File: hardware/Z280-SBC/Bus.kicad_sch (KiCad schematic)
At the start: 5 parts, among them J4 ATF-JTAG-10, J5 Conn_02x10_Odd_Even, J6 ADBUS, J7 SIGBUS, U10 ATF1504AS-10JU84

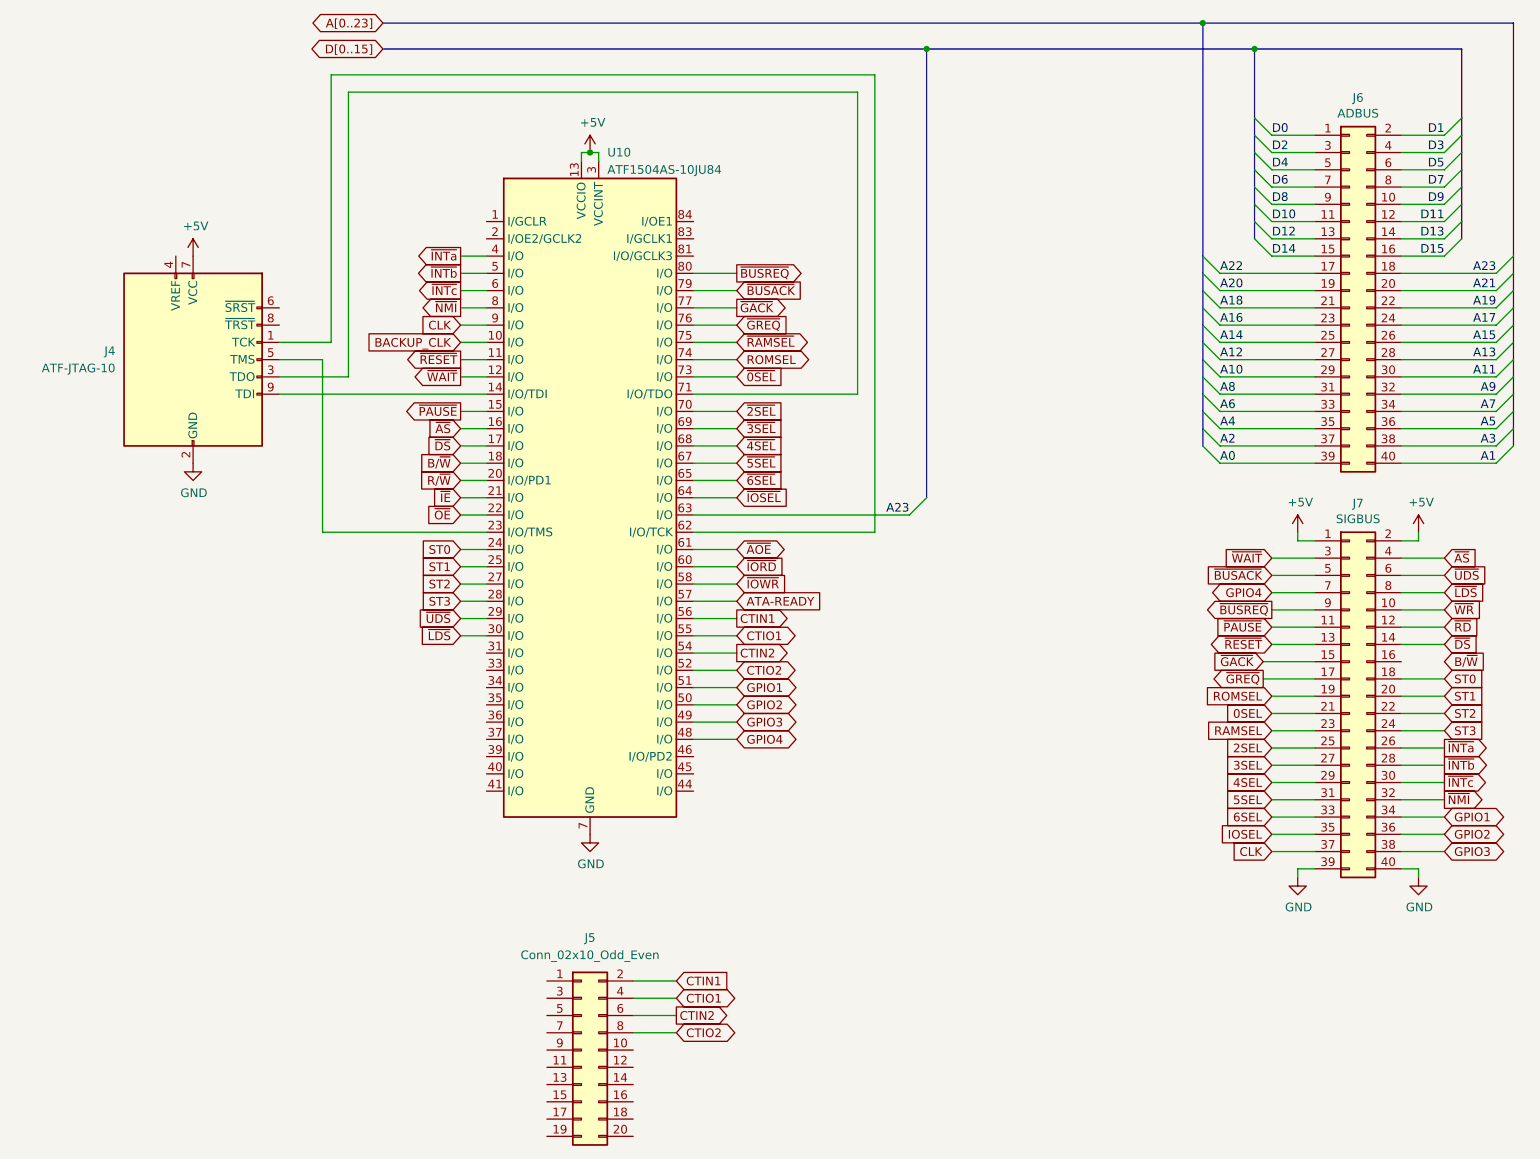
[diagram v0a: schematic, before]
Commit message: Work in progress on PCB design, address and data buses mostly connected
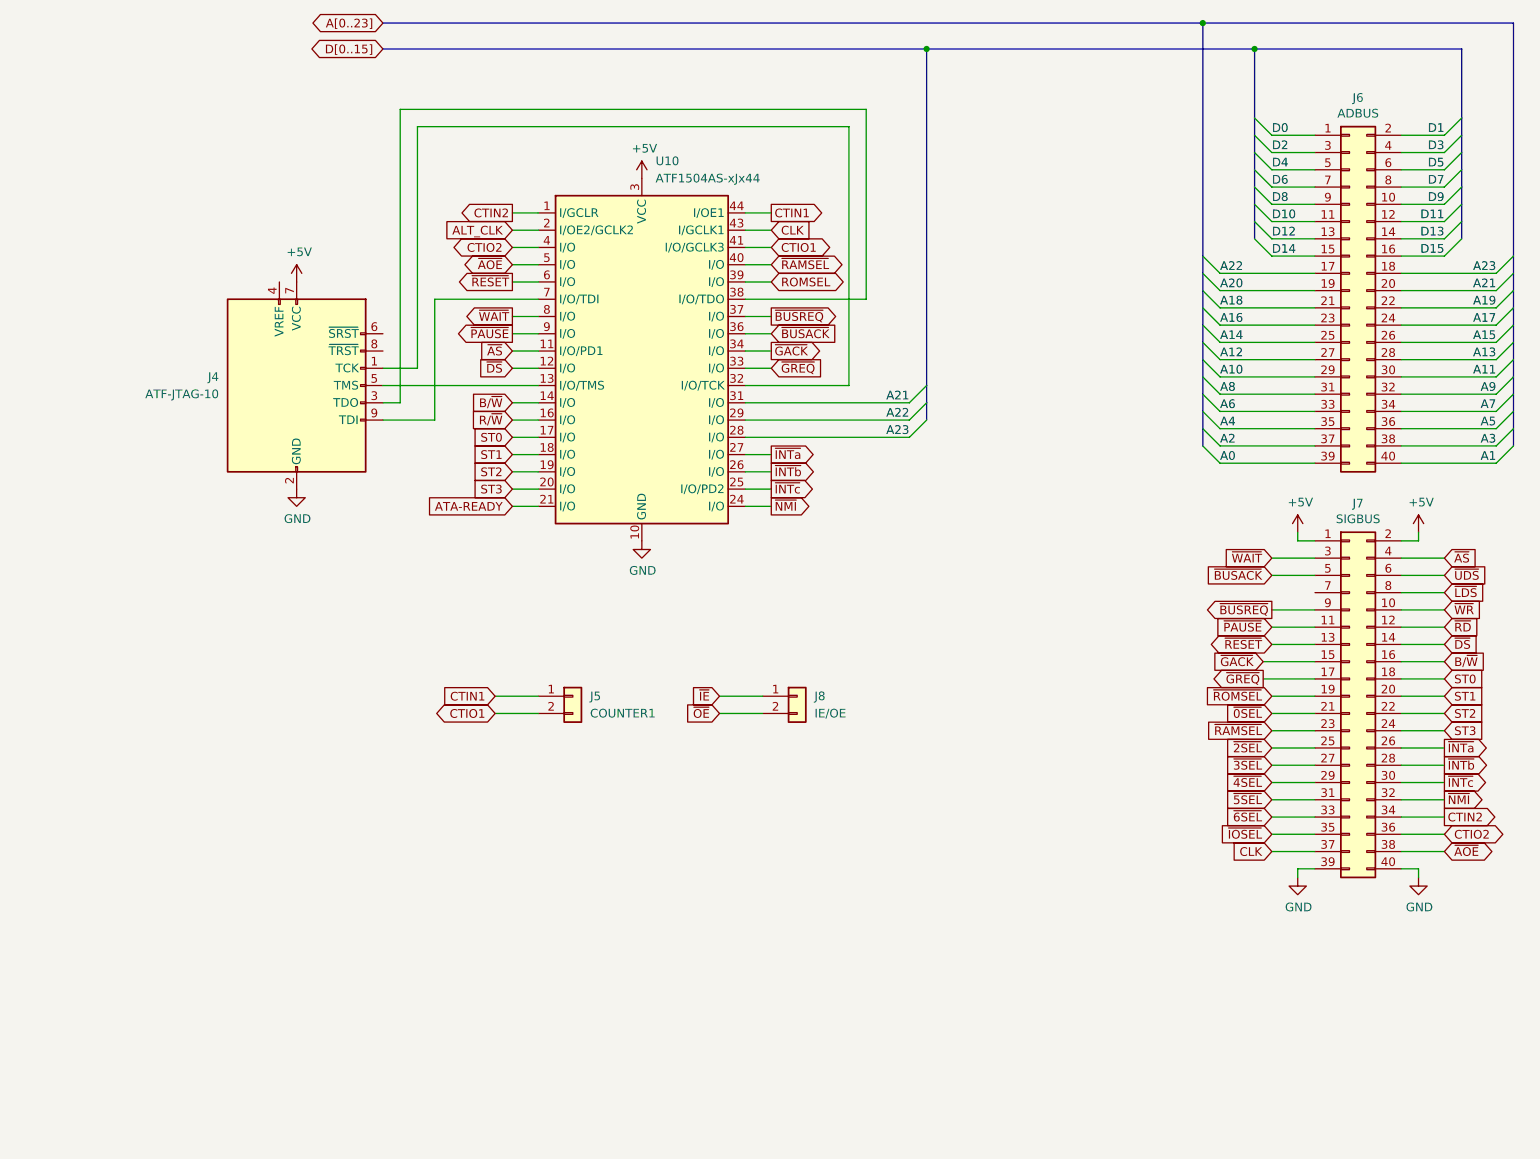
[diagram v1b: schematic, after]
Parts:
- removed J5: Conn_02x10_Odd_Even, Connector_PinHeader_2.54mm:PinHeader_2x10_P2.54mm_Vertical, symbol Connector_Generic:Conn_02x10_Odd_Even
- removed U10: ATF1504AS-10JU84, Package_LCC:PLCC-84_THT-Socket, symbol Z280:ATF1504AS-10JU84
- added J5: COUNTER1, Connector_PinHeader_2.54mm:PinHeader_1x02_P2.54mm_Vertical, symbol Connector_Generic:Conn_01x02
- added J8: IE/OE, Connector_PinHeader_2.54mm:PinHeader_1x02_P2.54mm_Vertical, symbol Connector_Generic:Conn_01x02
- added U10: ATF1504AS-xJx44, Package_LCC:PLCC-44_THT-Socket, symbol Z280:ATF1504AS-xJx44
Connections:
- net 0SEL is gone; now on net ~{0SEL}: J7.21 (Pin_21)
- net 2SEL is gone; now on net ~{2SEL}: J7.25 (Pin_25)
- net 3SEL is gone; now on net ~{3SEL}: J7.27 (Pin_27)
- net 4SEL is gone; now on net ~{4SEL}: J7.29 (Pin_29)
- net 5SEL is gone; now on net ~{5SEL}: J7.31 (Pin_31)
- net 6SEL is gone; now on net ~{6SEL}: J7.33 (Pin_33)
- net GPIO1 is gone; now on net CTIN2: J7.34 (Pin_34)
- net GPIO2 is gone; now on net CTIO2: J7.36 (Pin_36)
- net GPIO3 is gone; now on net ~{AOE}: J7.38 (Pin_38)
- net IOSEL is gone; now on net ~{IOSEL}: J7.35 (Pin_35)
- net RAMSEL is gone; now on net ~{RAMSEL}: J7.23 (Pin_23)
- net +5V: now also U10.15 (VCC), U10.23 (VCC), U10.3 (VCC), U10.35 (VCC)
- net A21: now also U10.31 (I/O)
- net A22: now also U10.29 (I/O)
- net A23: now also U10.28 (I/O)
- net ATA-READY: now also U10.21 (I/O)
- net B/~{W}: now also J7.16 (Pin_16), U10.14 (I/O)
- net CLK: now also U10.43 (I/GCLK1)
- net CTIN1: now also J5.1 (Pin_1), U10.44 (I/OE1)
- net CTIN2: now also U10.1 (I/GCLR)
- net CTIO1: now also J5.2 (Pin_2), U10.41 (I/O/GCLK3)
- net CTIO2: now also U10.4 (I/O)
- net GND: now also U10.10 (GND), U10.22 (GND), U10.30 (GND), U10.42 (GND)
- net ROMSEL: now also U10.39 (I/O); no longer J7.19 (Pin_19)
- net R/~{W}: now also U10.16 (I/O)
- net ST0: now also U10.17 (I/O)
- net ST1: now also U10.18 (I/O)
- net ST2: now also U10.19 (I/O)
- net ST3: now also U10.20 (I/O)
- net ~{AOE}: now also U10.5 (I/O)
- net ~{AS}: now also U10.11 (I/O/PD1)
- net ~{BUSACK}: now also U10.36 (I/O)
- net ~{BUSREQ}: now also U10.37 (I/O)
- net ~{DS}: now also U10.12 (I/O)
- net ~{GACK}: now also U10.34 (I/O)
- net ~{GREQ}: now also U10.33 (I/O)
- net ~{IE}: now also J8.1 (Pin_1)
- net ~{INTa}: now also U10.27 (I/O)
- net ~{INTb}: now also U10.26 (I/O)
- net ~{INTc}: now also U10.25 (I/O/PD2)
- net ~{NMI}: now also U10.24 (I/O)
- net ~{OE}: now also J8.2 (Pin_2)
- net ~{PAUSE}: now also U10.9 (I/O)
- net ~{RAMSEL}: now also U10.40 (I/O)
- net ~{RESET}: now also U10.6 (I/O)
- net ~{WAIT}: now also U10.8 (I/O)
- net at J4.9 (TDI): now also U10.7 (I/O/TDI)
- net at J4.5 (TMS): now also U10.13 (I/O/TMS)
- net at J4.1 (TCK): now also U10.32 (I/O/TCK)
- net at J4.3 (TDO): now also U10.38 (I/O/TDO)
- net GPIO4: no longer names the net of J7.7 (Pin_7)
- new net ALT_CLK: U10.2 (I/OE2/GCLK2)
- new net ~{ROMSEL}: J7.19 (Pin_19)
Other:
- moved on the sheet: J4

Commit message: Rev1 - All connections completed
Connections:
- net ROMSEL is gone; now on net ~{ROMSEL}: U10.39 (I/O)
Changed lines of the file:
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@@
     )
   )
-  (global_label "ROMSEL" (shape bidirectional) (at 128.27 60.96 0) (fields_autoplaced)
+  (global_label "~{ROMSEL}" (shape bidirectional) (at 128.27 60.96 0) (fields_autoplaced)
     (effects (font (size 1.27 1.27)) (justify left))
     (property "Intersheet References" "${INTERSHEET_REFS}" (id 0) (at 138.1217 60.8806 0)

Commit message: Z280-SBC Revision 1 is complete
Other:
- title: (none) -> Z280-SBC
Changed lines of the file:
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@@
 (kicad_sch (version 20211123) (generator eeschema)
   (paper "A4")
+  (title_block
+    (title "Z280-SBC")
+    (rev "1")
+  )
   (junction (at 191.77 22.86) (diameter 0) (color 0 0 0 0)
   )

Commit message: Fixed most of the issues with Rev.1
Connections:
- net ALT_CLK renamed SERCLK
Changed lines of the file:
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@@
   (title_block
     (title "Z280-SBC")
-    (rev "1")
+    (rev "2")
   )
   (junction (at 191.77 22.86) (diameter 0) (color 0 0 0 0)
@@
     )
   )
-  (global_label "ALT_CLK" (shape input) (at 90.17 53.34 180) (fields_autoplaced)
+  (global_label "SERCLK" (shape input) (at 90.17 53.34 180) (fields_autoplaced)
     (effects (font (size 1.27 1.27)) (justify right))
-    (property "Intersheet References" "${INTERSHEET_REFS}" (id 0) (at 80.1369 53.2606 0)
+    (property "Intersheet References" "${INTERSHEET_REFS}" (id 0) (at 80.5602 53.2606 0)
       (effects (font (size 1.27 1.27)) (justify right) hide)
     )

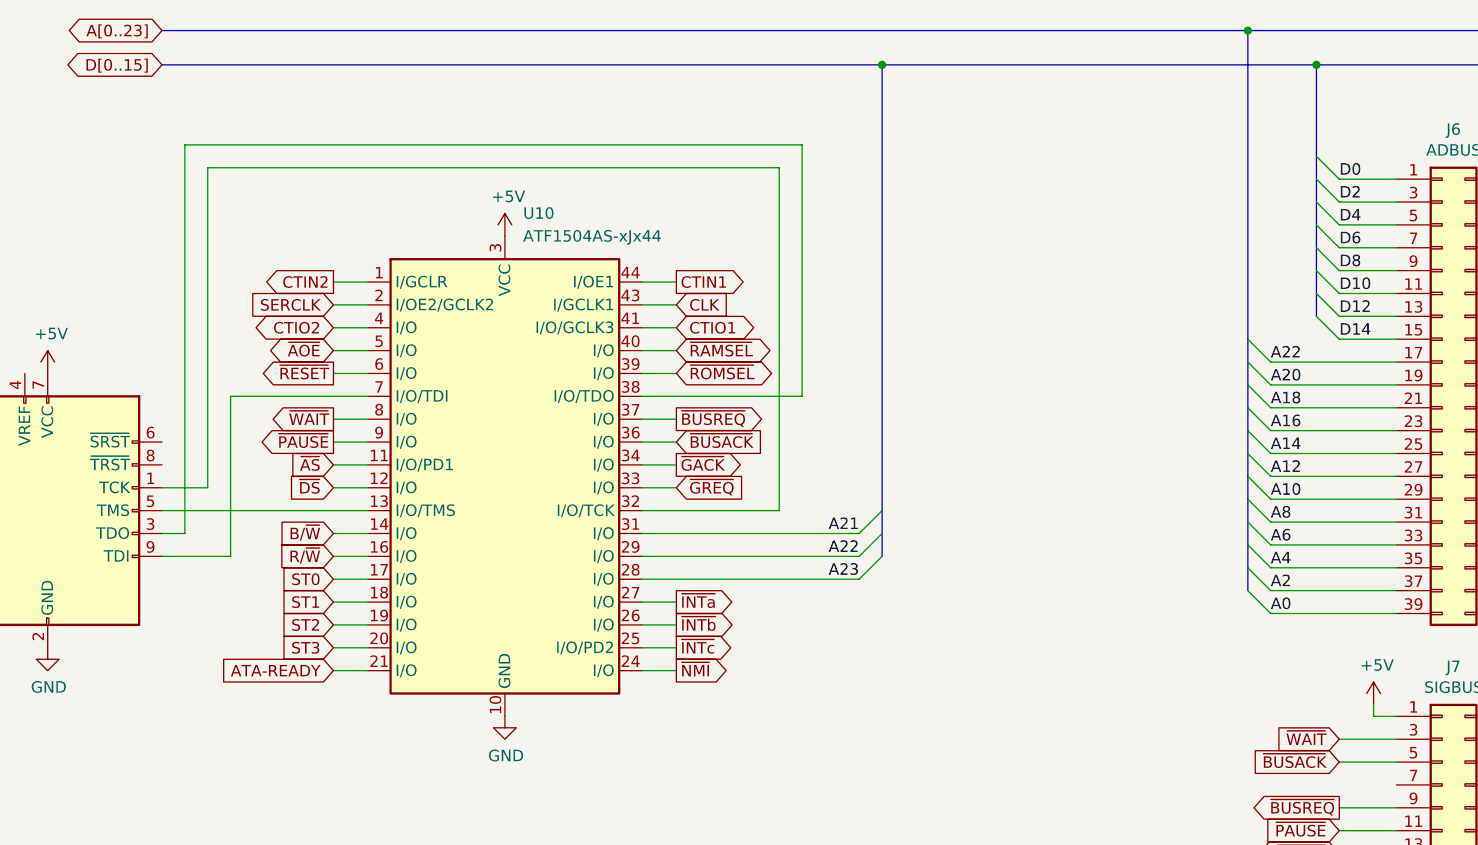
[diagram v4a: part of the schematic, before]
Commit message: Moved the CTIN pins to output pins on the CPLD
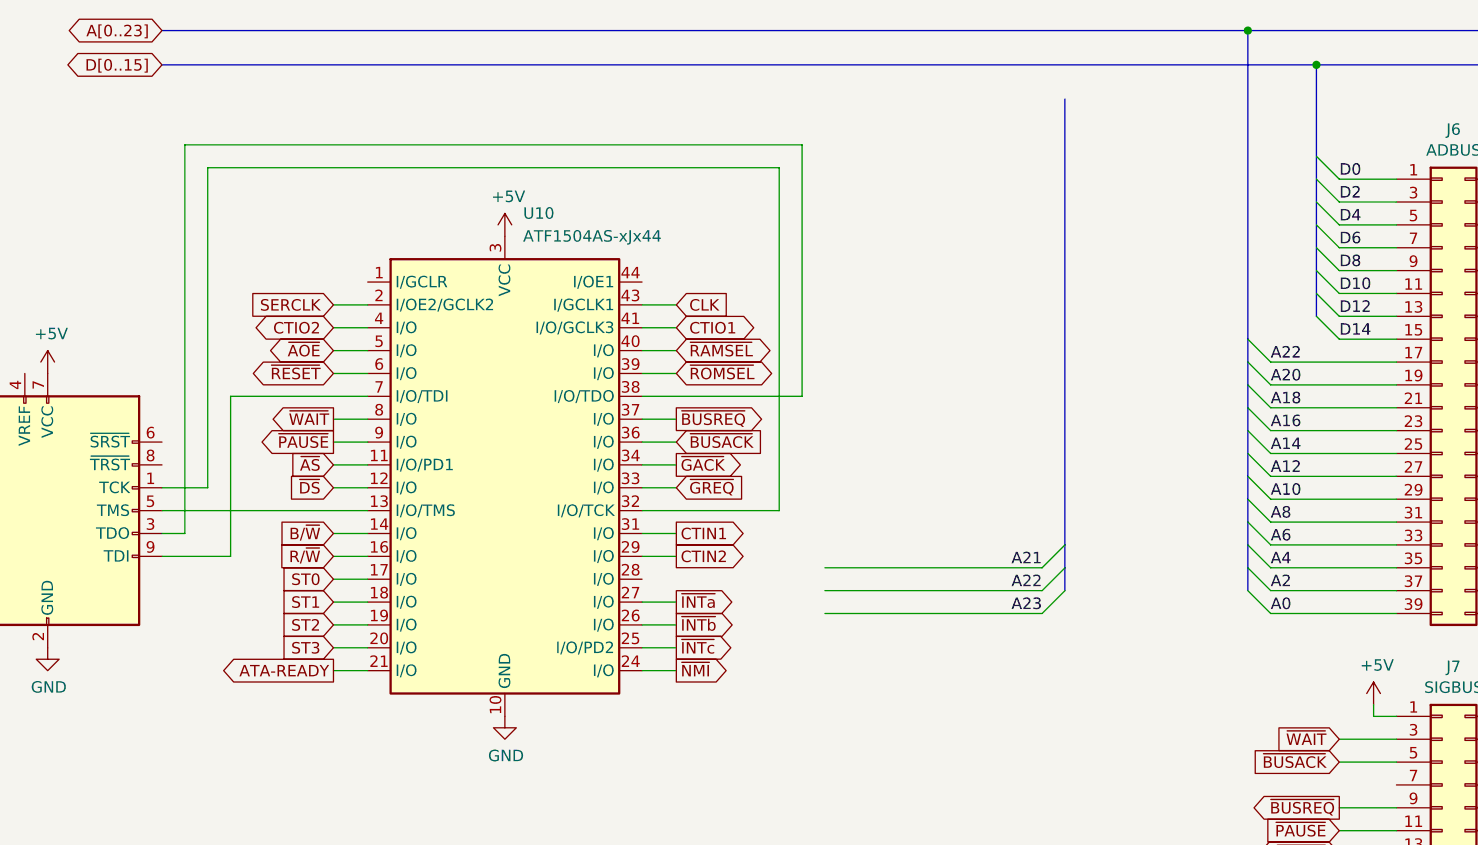
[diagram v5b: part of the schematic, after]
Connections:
- net A21: no longer U10.31 (I/O)
- net A22: no longer U10.29 (I/O)
- net A23: no longer U10.28 (I/O)
- net CTIN1: now also U10.31 (I/O); no longer U10.44 (I/OE1)
- net CTIN2: now also U10.29 (I/O); no longer U10.1 (I/GCLR)
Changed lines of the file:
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@@
   (junction (at 191.77 22.86) (diameter 0) (color 0 0 0 0)
   )
-  (junction (at 151.13 26.67) (diameter 0) (color 0 0 0 0)
-  )
   (junction (at 199.39 26.67) (diameter 0) (color 0 0 0 0)
   )
@@
     (stroke (width 0) (type default) (color 0 0 0 0))
   )
-  (bus_entry (at 148.59 81.28) (size 2.54 -2.54)
+  (bus_entry (at 168.91 85.09) (size 2.54 -2.54)
     (stroke (width 0) (type default) (color 0 0 0 0))
   )
@@
     (stroke (width 0) (type default) (color 0 0 0 0))
   )
-  (bus_entry (at 148.59 78.74) (size 2.54 -2.54)
+  (bus_entry (at 168.91 82.55) (size 2.54 -2.54)
     (stroke (width 0) (type default) (color 0 0 0 0))
   )
@@
     (stroke (width 0) (type default) (color 0 0 0 0))
   )
-  (bus_entry (at 148.59 83.82) (size 2.54 -2.54)
+  (bus_entry (at 168.91 87.63) (size 2.54 -2.54)
     (stroke (width 0) (type default) (color 0 0 0 0))
   )
@@
     (stroke (width 0) (type default) (color 0 0 0 0))
   )
-  (wire (pts (xy 124.46 81.28) (xy 148.59 81.28))
+  (wire (pts (xy 144.78 85.09) (xy 168.91 85.09))
     (stroke (width 0) (type default) (color 0 0 0 0))
   )
@@
     (stroke (width 0) (type default) (color 0 0 0 0))
   )
-  (bus (pts (xy 71.12 26.67) (xy 151.13 26.67))
-    (stroke (width 0) (type default) (color 0 0 0 0))
-  )
   (wire (pts (xy 223.52 147.32) (xy 223.52 148.59))
     (stroke (width 0) (type default) (color 0 0 0 0))
@@
     (stroke (width 0) (type default) (color 0 0 0 0))
   )
-  (bus (pts (xy 151.13 26.67) (xy 199.39 26.67))
+  (bus (pts (xy 71.12 26.67) (xy 199.39 26.67))
     (stroke (width 0) (type default) (color 0 0 0 0))
   )
@@
     (stroke (width 0) (type default) (color 0 0 0 0))
   )
-  (bus (pts (xy 151.13 78.74) (xy 151.13 81.28))
+  (bus (pts (xy 171.45 82.55) (xy 171.45 85.09))
     (stroke (width 0) (type default) (color 0 0 0 0))
   )
@@
     (stroke (width 0) (type default) (color 0 0 0 0))
   )
-  (wire (pts (xy 124.46 78.74) (xy 148.59 78.74))
+  (wire (pts (xy 144.78 82.55) (xy 168.91 82.55))
     (stroke (width 0) (type default) (color 0 0 0 0))
   )
@@
     (stroke (width 0) (type default) (color 0 0 0 0))
   )
-  (bus (pts (xy 151.13 76.2) (xy 151.13 78.74))
+  (bus (pts (xy 171.45 80.01) (xy 171.45 82.55))
     (stroke (width 0) (type default) (color 0 0 0 0))
   )
@@
     (stroke (width 0) (type default) (color 0 0 0 0))
   )
-  (wire (pts (xy 124.46 83.82) (xy 148.59 83.82))
+  (wire (pts (xy 144.78 87.63) (xy 168.91 87.63))
     (stroke (width 0) (type default) (color 0 0 0 0))
   )
@@
     (stroke (width 0) (type default) (color 0 0 0 0))
   )
-  (bus (pts (xy 151.13 26.67) (xy 151.13 76.2))
+  (bus (pts (xy 171.45 30.48) (xy 171.45 80.01))
     (stroke (width 0) (type default) (color 0 0 0 0))
   )
@@
     (stroke (width 0) (type default) (color 0 0 0 0))
   )
-  (wire (pts (xy 124.46 50.8) (xy 128.27 50.8))
+  (wire (pts (xy 124.46 78.74) (xy 128.27 78.74))
     (stroke (width 0) (type default) (color 0 0 0 0))
   )
@@
     (stroke (width 0) (type default) (color 0 0 0 0))
   )
-  (wire (pts (xy 93.98 50.8) (xy 90.17 50.8))
+  (wire (pts (xy 124.46 81.28) (xy 128.27 81.28))
     (stroke (width 0) (type default) (color 0 0 0 0))
   )
@@
     (effects (font (size 1.27 1.27)) (justify left bottom))
   )
-  (label "A21" (at 148.59 78.74 180)
-    (effects (font (size 1.27 1.27)) (justify right bottom))
-  )
-  (label "A22" (at 148.59 81.28 180)
+  (label "A21" (at 168.91 82.55 180)
+    (effects (font (size 1.27 1.27)) (justify right bottom))
+  )
+  (label "A22" (at 168.91 85.09 180)
     (effects (font (size 1.27 1.27)) (justify right bottom))
   )
@@
     (effects (font (size 1.27 1.27)) (justify left bottom))
   )
-  (label "A23" (at 148.59 83.82 180)
+  (label "A23" (at 168.91 87.63 180)
     (effects (font (size 1.27 1.27)) (justify right bottom))
   )
@@
     )
   )
-  (global_label "ATA-READY" (shape input) (at 90.17 93.98 180) (fields_autoplaced)
+  (global_label "ATA-READY" (shape output) (at 90.17 93.98 180) (fields_autoplaced)
     (effects (font (size 1.27 1.27)) (justify right))
     (property "Intersheet References" "${INTERSHEET_REFS}" (id 0) (at 77.1736 93.9006 0)
@@
     )
   )
-  (global_label "CTIN2" (shape output) (at 90.17 50.8 180) (fields_autoplaced)
-    (effects (font (size 1.27 1.27)) (justify right))
-    (property "Intersheet References" "${INTERSHEET_REFS}" (id 0) (at 82.3745 50.7206 0)
-      (effects (font (size 1.27 1.27)) (justify right) hide)
+  (global_label "CTIN2" (shape output) (at 128.27 81.28 0) (fields_autoplaced)
+    (effects (font (size 1.27 1.27)) (justify left))
+    (property "Intersheet References" "${INTERSHEET_REFS}" (id 0) (at 136.0655 81.2006 0)
+      (effects (font (size 1.27 1.27)) (justify left) hide)
     )
   )
@@
     )
   )
-  (global_label "CTIN1" (shape output) (at 128.27 50.8 0) (fields_autoplaced)
-    (effects (font (size 1.27 1.27)) (justify left))
-    (property "Intersheet References" "${INTERSHEET_REFS}" (id 0) (at 136.0655 50.7206 0)
+  (global_label "CTIN1" (shape output) (at 128.27 78.74 0) (fields_autoplaced)
+    (effects (font (size 1.27 1.27)) (justify left))
+    (property "Intersheet References" "${INTERSHEET_REFS}" (id 0) (at 136.0655 78.6606 0)
       (effects (font (size 1.27 1.27)) (justify left) hide)
     )
@@
     )
   )
-  (global_label "~{RESET}" (shape output) (at 90.17 60.96 180) (fields_autoplaced)
+  (global_label "~{RESET}" (shape bidirectional) (at 90.17 60.96 180) (fields_autoplaced)
     (effects (font (size 1.27 1.27)) (justify right))
     (property "Intersheet References" "${INTERSHEET_REFS}" (id 0) (at 82.0117 60.8806 0)
